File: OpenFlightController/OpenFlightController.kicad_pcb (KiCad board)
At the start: 2 copper layers, 37.4 x 37.4 mm, 3 parts, among them U1 STM32F405RGT6, U2 MAX7456EUI+

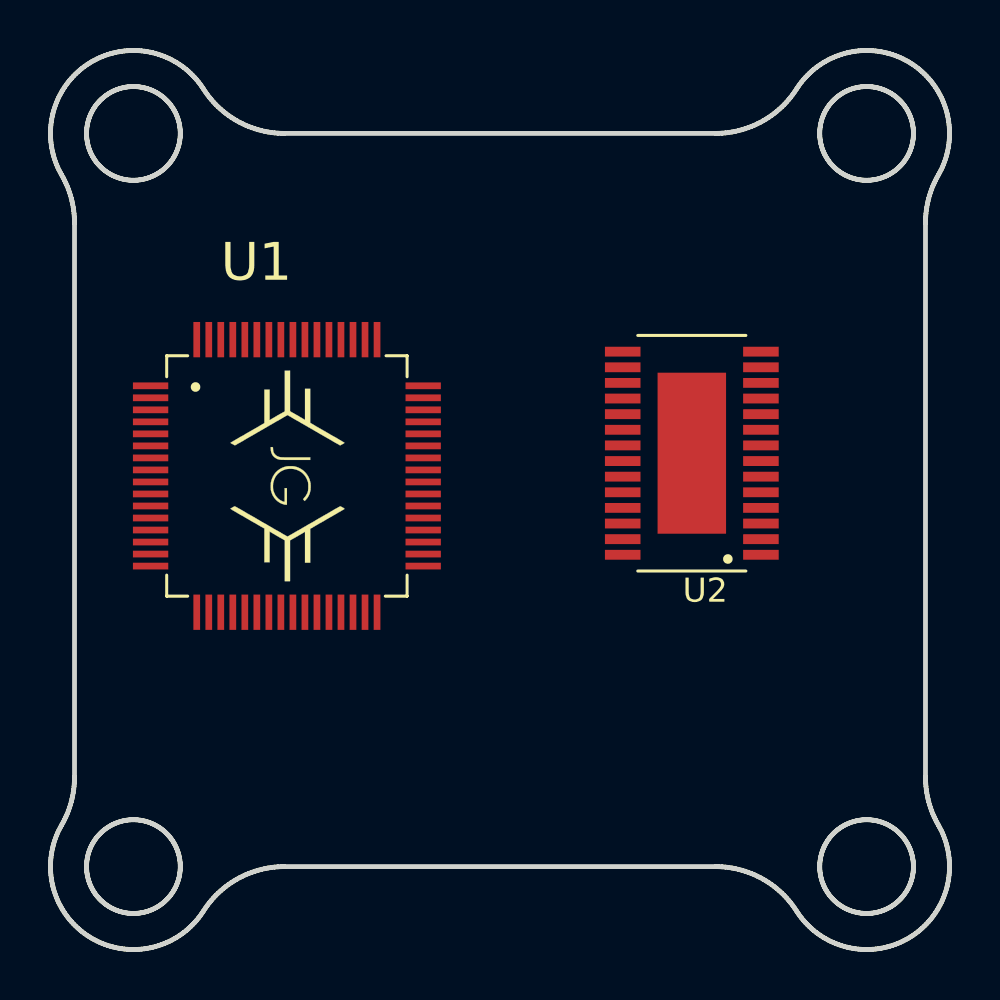
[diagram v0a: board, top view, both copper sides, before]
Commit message: Add Power In 3v3
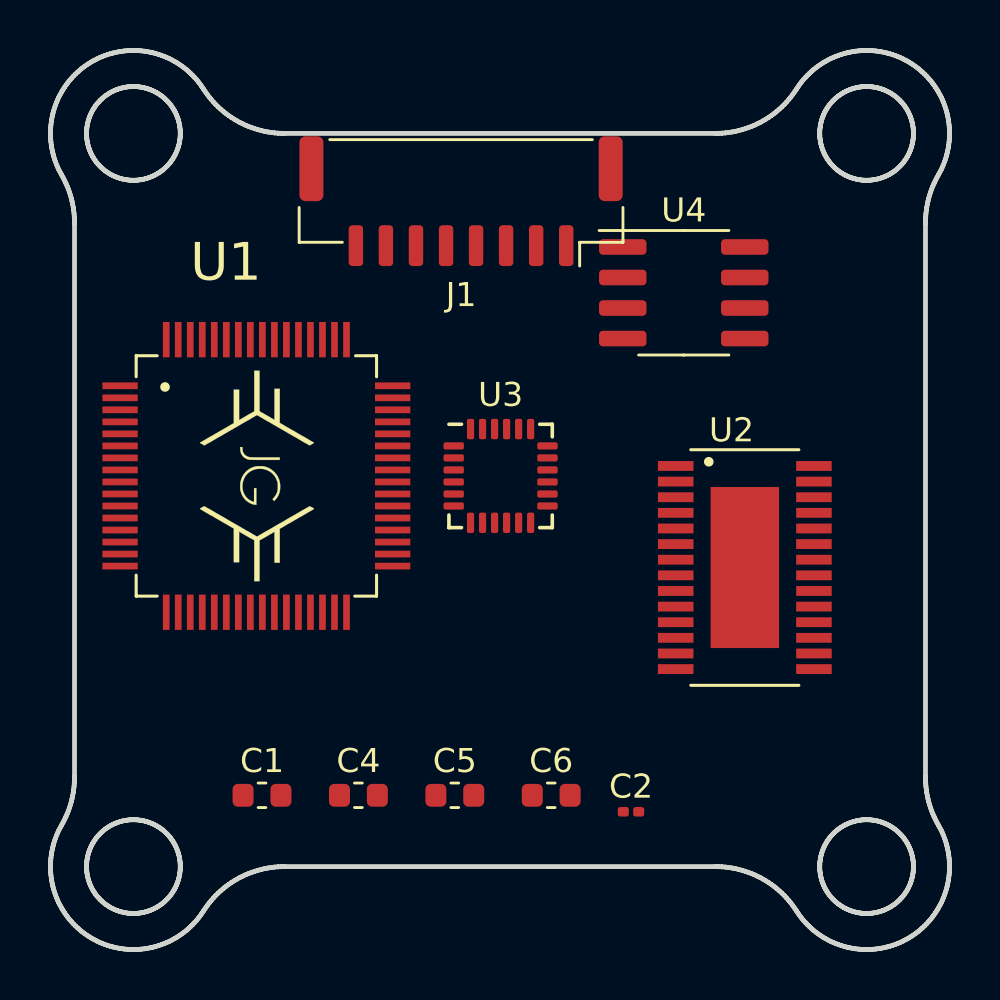
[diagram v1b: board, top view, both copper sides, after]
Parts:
- added C1: 1µF, Capacitor_SMD:C_0603_1608Metric, F.Cu at (122.2, 85.7)
- added C2: 0.01µF, Capacitor_SMD:C_0201_0603Metric, F.Cu at (137.5, 86.4)
- added C4: 0.1µF, Capacitor_SMD:C_0603_1608Metric, F.Cu at (126.2, 85.7)
- added C5: 2.2nf, Capacitor_SMD:C_0603_1608Metric, F.Cu at (130.2, 85.7)
- added C6: 0.1µF, Capacitor_SMD:C_0603_1608Metric, F.Cu at (134.2, 85.7)
- added J1: Conn_01x08_Male, Connector_JST:JST_GH_SM08B-GHS-TB_1x08-1MP_P1.25mm_Horizontal, F.Cu at (130.4, 61.0)
- added U3: MPU-6000, Sensor_Motion:InvenSense_QFN-24_4x4mm_P0.5mm, F.Cu at (132.1, 72.4)
- added U4: LT1763-3.3, Package_SO:SOP-8_3.76x4.96mm_P1.27mm, F.Cu at (139.7, 64.8)
- moved U2 5.24 mm to (142.2, 76.2), turned to 0 degrees
- moved G*** 1.27 mm to (121.9, 72.4)
- moved U1 1.27 mm to (121.9, 72.4)
